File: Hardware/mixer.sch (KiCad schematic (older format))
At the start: 18 parts, among them J2 Audio-Jack-2_Switch, U4 TL074

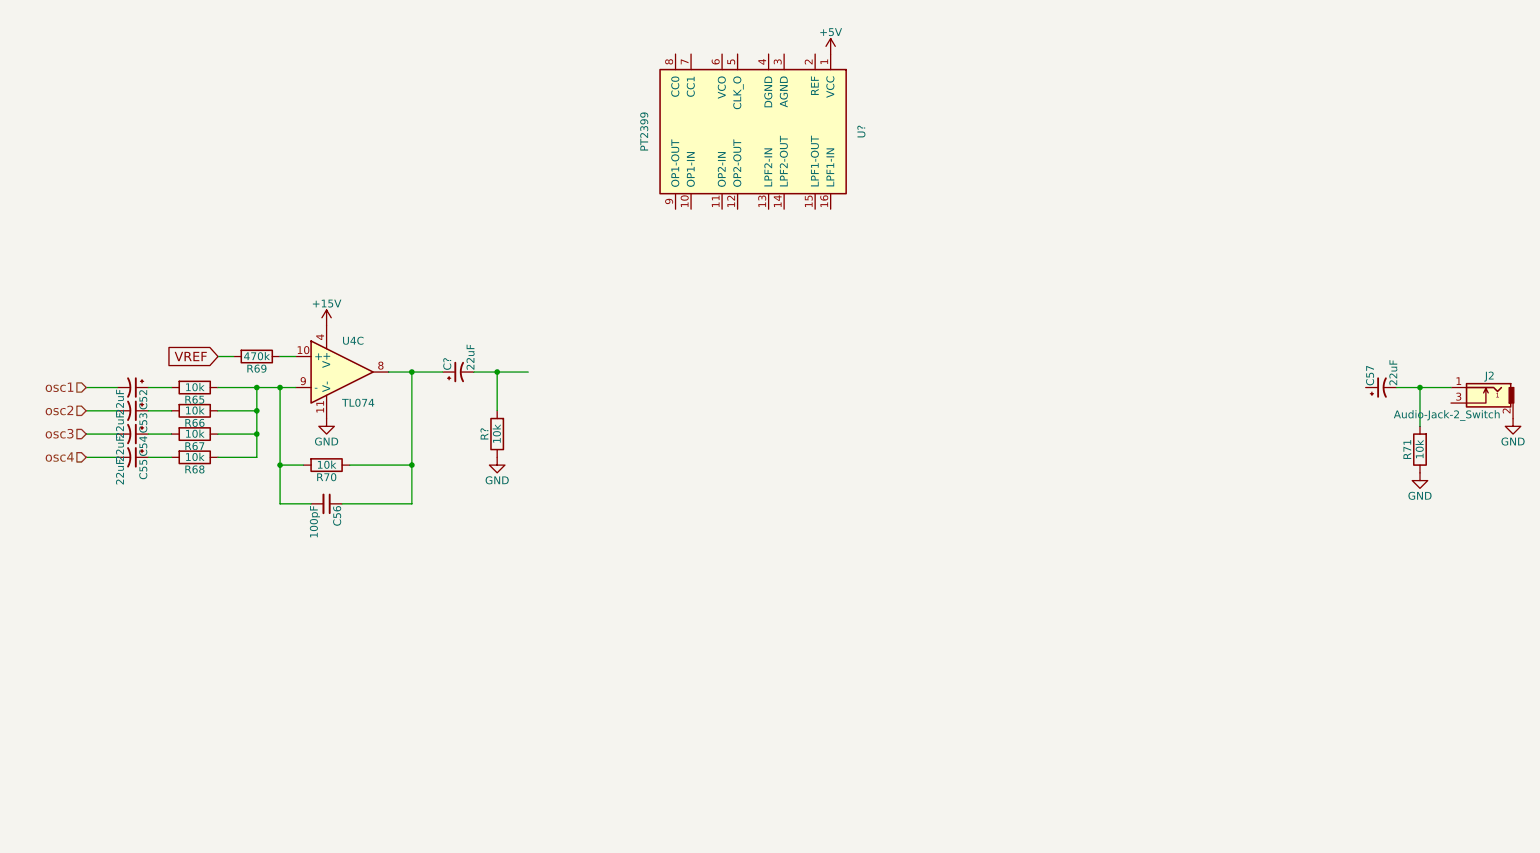
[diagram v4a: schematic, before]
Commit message: add initial delay schematic based on PT2399 application circuit.
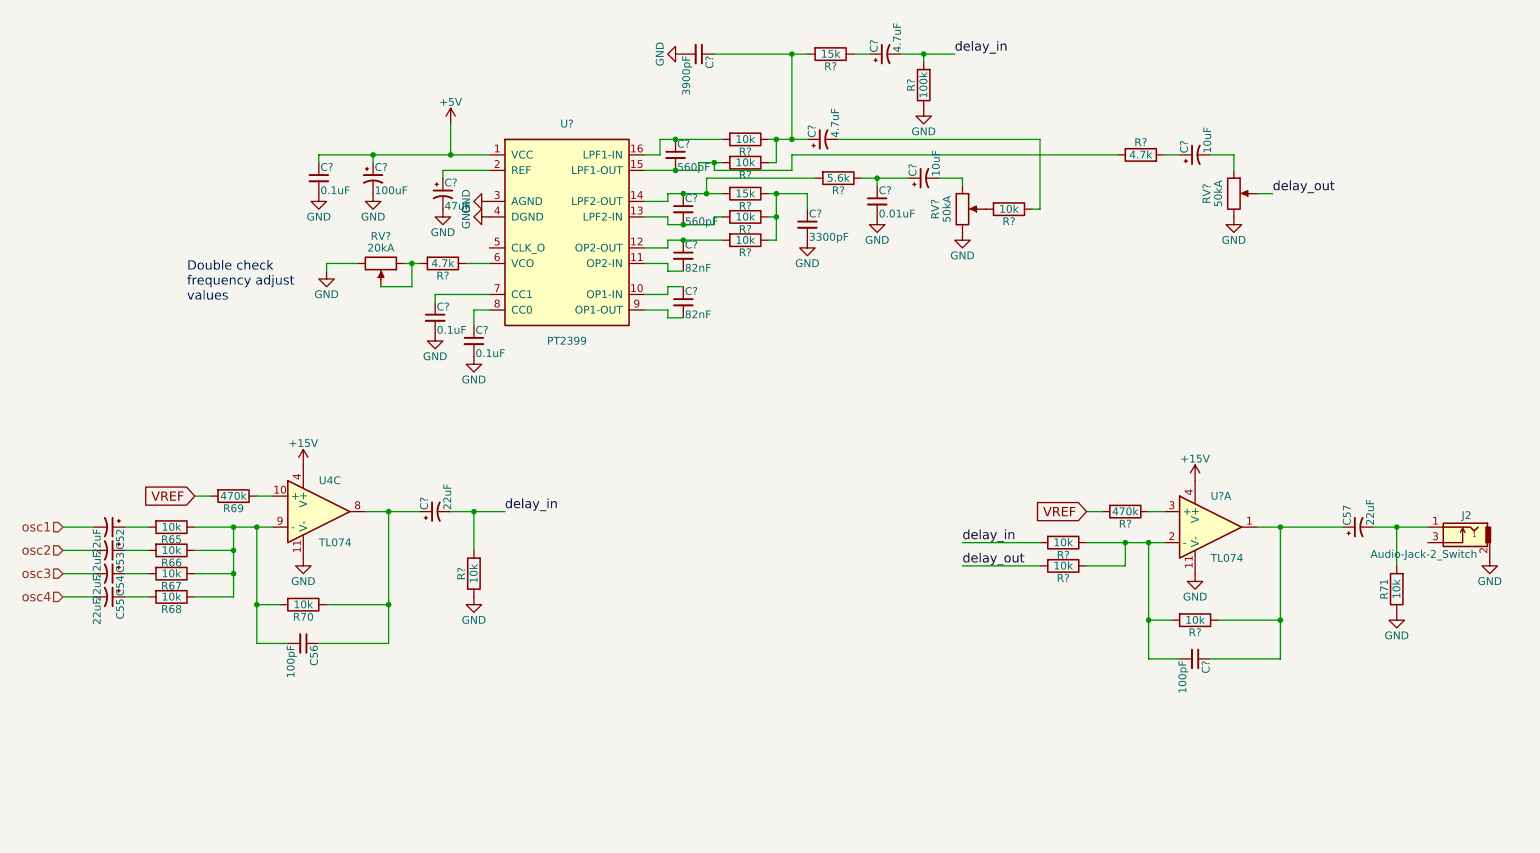
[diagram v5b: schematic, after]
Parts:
- added C?: 100uF, symbol CP1_Small
- added C? (x3): 0.1uF, symbol C_Small
- added C?: 47uF, symbol CP1_Small
- added C? (x2): 82nF, symbol C_Small
- added C? (x2): 560pF, symbol C_Small
- added C?: 3300pF, symbol C_Small
- added C?: 0.01uF, symbol C_Small
- added C? (x2): 10uF, symbol CP1_Small
- added C? (x2): 4.7uF, symbol CP1_Small
- added C?: 3900pF, symbol C_Small
- added C?: 100pF, digikey-footprints:0805, symbol C_Small
- added R? (x2): 4.7k, symbol R
- added R? (x5): 10k, symbol R
- added R? (x2): 15k, symbol R
- added R?: 5.6k, symbol R
- added R?: 100k, symbol R
- added R? (x3): 10k, digikey-footprints:0805, symbol R
- added R?: 470k, digikey-footprints:0805, symbol R
- added RV?: 20kA, symbol POT
- added RV? (x2): 50kA, symbol POT
- added U?: TL074, digikey-footprints:SOIC-14_W3.9mm, symbol TL074
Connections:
- net labels added: delay_in, delay_out
- wire segments 26 -> 143
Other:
- note added: "Double check \nfrequency adjust \nvalues"
- moved on the sheet: C52, C53, C54, C55, C56, C57, C?, J2, R65, R66, R67, R68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

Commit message: change delay summing to balance control to allow 0-100% wet signal, rather than 0-50%.
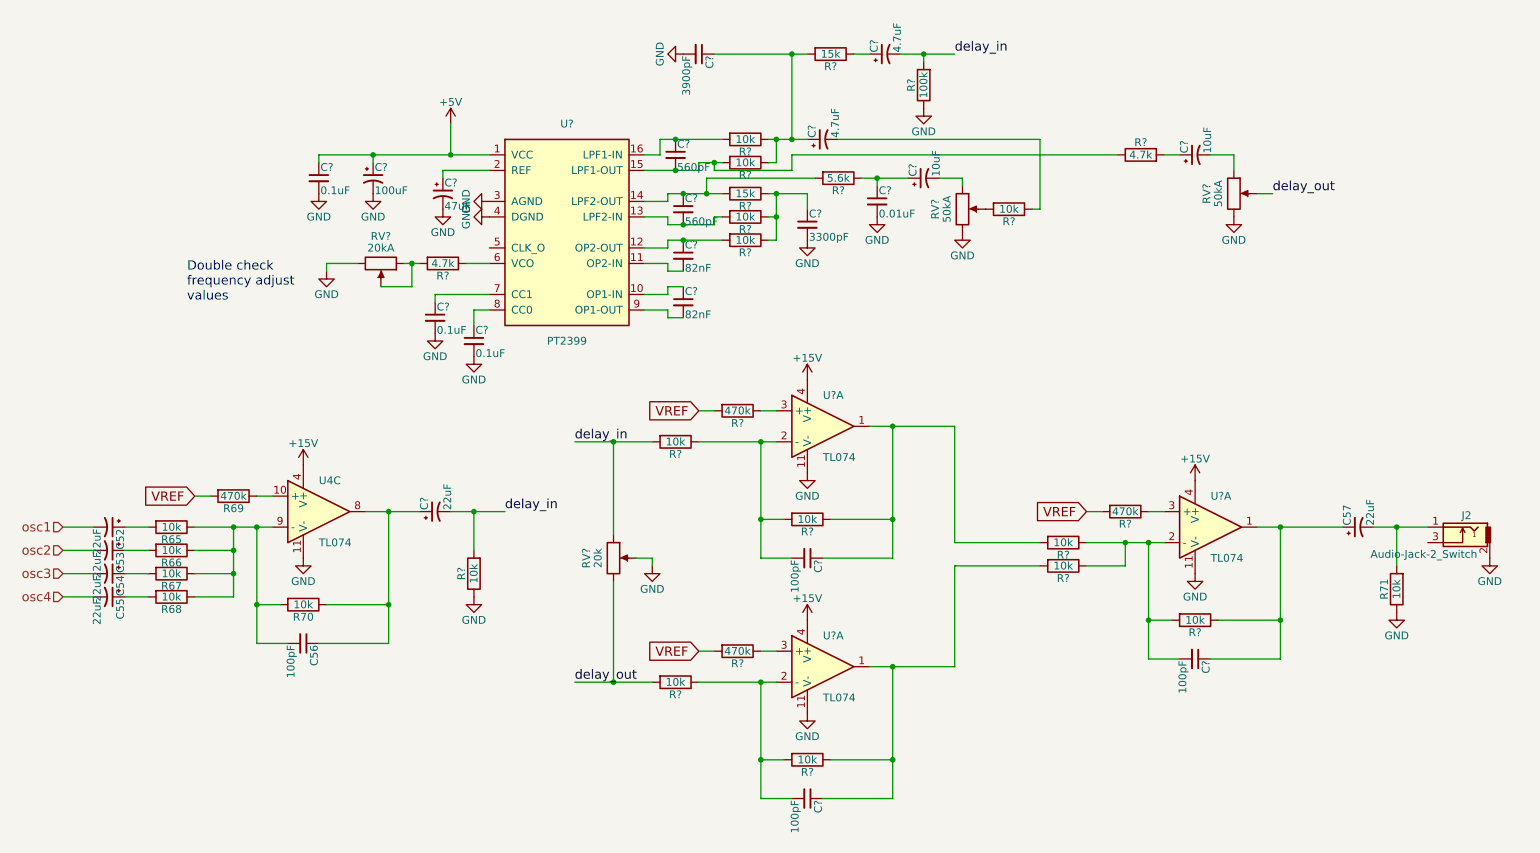
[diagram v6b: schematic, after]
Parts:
- added C? (x2): 100pF, digikey-footprints:0805, symbol C_Small
- added R? (x4): 10k, digikey-footprints:0805, symbol R
- added R? (x2): 470k, digikey-footprints:0805, symbol R
- added RV?: 20k, symbol POT
- added U? (x2): TL074, digikey-footprints:SOIC-14_W3.9mm, symbol TL074
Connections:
- net +15V: now also U?.4 (V+), U?.4 (V+)
- net GND: now also RV?.2, U?.11 (V-), U?.11 (V-)
- net VREF: now also R?.2, R?.2
- net delay_in: now also R?.2, RV?.1; no longer R?.2
- net delay_out: now also R?.2, RV?.3; no longer R?.2
- new net: C?.1, R?.1, R?.2, U?.1 (x2)
- new net: C?.2, R?.1, R?.2, U?.2 (-) (x2)
- new net: R?.1, U?.3 (+) (x2)

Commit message: begin PCB v2 layout. fix ref designators, associate footprints on new components, create new PCB file, import components.
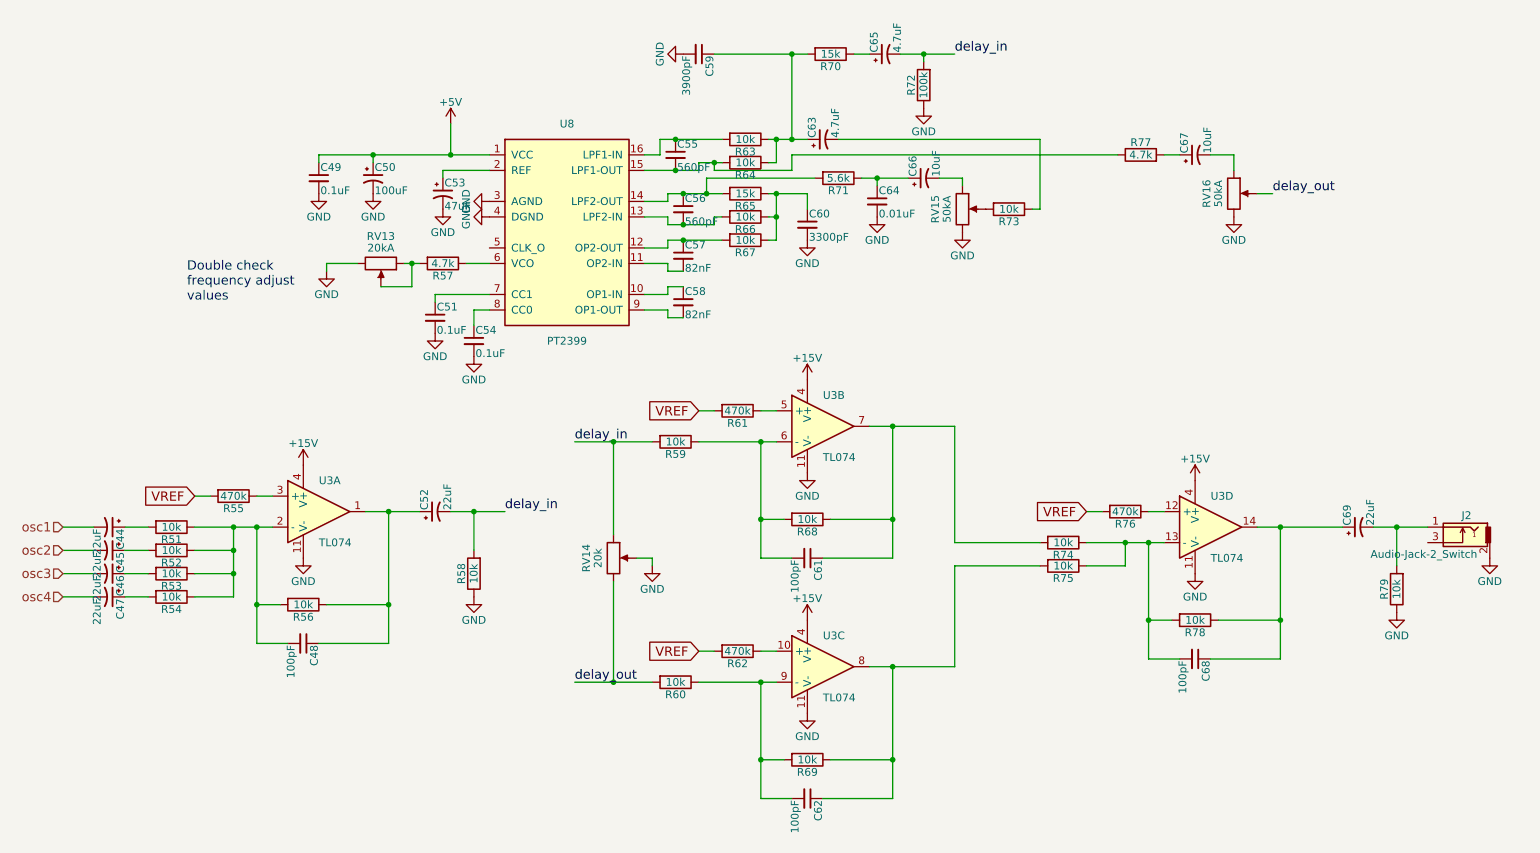
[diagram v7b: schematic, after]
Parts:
- gave numbers to parts that had none: 48
- renumbered C52 to C44, C53 to C45, C54 to C46, C55 to C47, C56 to C48, C57 to C69, R65 to R51, R66 to R52, R67 to R53, R68 to R54, R69 to R55, R70 to R56, R71 to R79, U4 to U3
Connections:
- net at C48.2, R51.1, R52.1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: now also U3.2 (-); no longer U3.9 (-)
- net at C48.1, C52.1, R56.1: now also U3.1; no longer U3.8
- net at C68.1, C69.1, R78.1: now also U3.14; no longer U3.1
- net at R55.1: now also U3.3 (+); no longer U3.10 (+)
- net at C68.2, R74.1, R75.1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: now also U3.13 (-); no longer U3.2 (-)
- net at C61.1, R68.1, R74.2: now also U3.7; no longer U3.1
- net at C62.1, R69.1, R75.2: now also U3.8; no longer U3.1
- net at R76.1: now also U3.12 (+); no longer U3.3 (+)
- net at C61.2, R59.1, R68.2: now also U3.6 (-); no longer U3.2 (-)
- net at R61.1: now also U3.5 (+); no longer U3.3 (+)
- net at C62.2, R60.1, R69.2: now also U3.9 (-); no longer U3.2 (-)
- net at R62.1: now also U3.10 (+); no longer U3.3 (+)
